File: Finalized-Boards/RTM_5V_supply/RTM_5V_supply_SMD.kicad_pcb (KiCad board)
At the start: 4 copper layers, 18.5 x 99 mm, 12 parts, among them J1 86093968114755V1LF

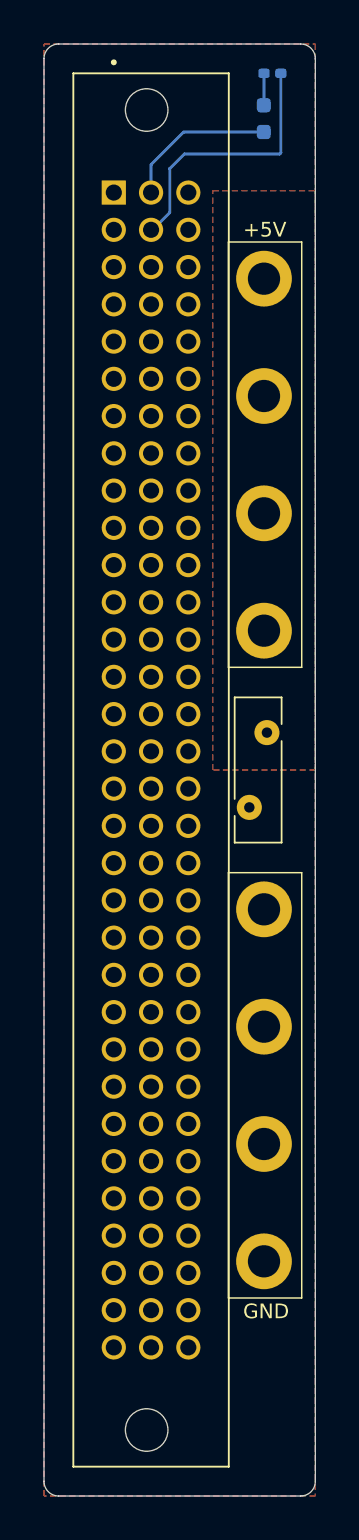
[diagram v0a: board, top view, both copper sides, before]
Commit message: Apply Matt's review changes to RTM, fanout and SRAM boards
SRAM: serial -> IDL_26_007 RevC - 09/2026 - CK/RS; vias untented (board-level);
GND zone 0.4 clearance / 0.1524 min width; In2 +3.3V stripe pulled back from
both board edges (tips 103.25 / 126.05) with 45-degree miters; +3.3V via moved
to (165.54, 125.92) and re-routed on F.Cu/B.Cu to clear GND (was 2 DRC errors);
C1/C2 0402 -> 0603 X7R in schematic and PCB; orphan teardrop + 2 zero-length
tracks removed.
Fanout: Matt's reworked layout (12 AWG input centred, both-side labels, 3 mm
shorter test points, D1/R1 as real reference designators, silk moved clear).
RTM: four 1812 1 A PPTCs, one per output; +5V pour full-board on F.Cu/In2,
GND on B.Cu/In1; 3.4 mm fused traces; zones extended past Edge.Cuts.
Removed stale pre-review gerbers/drills/layer PDFs (duplicates of Chris-Originals).
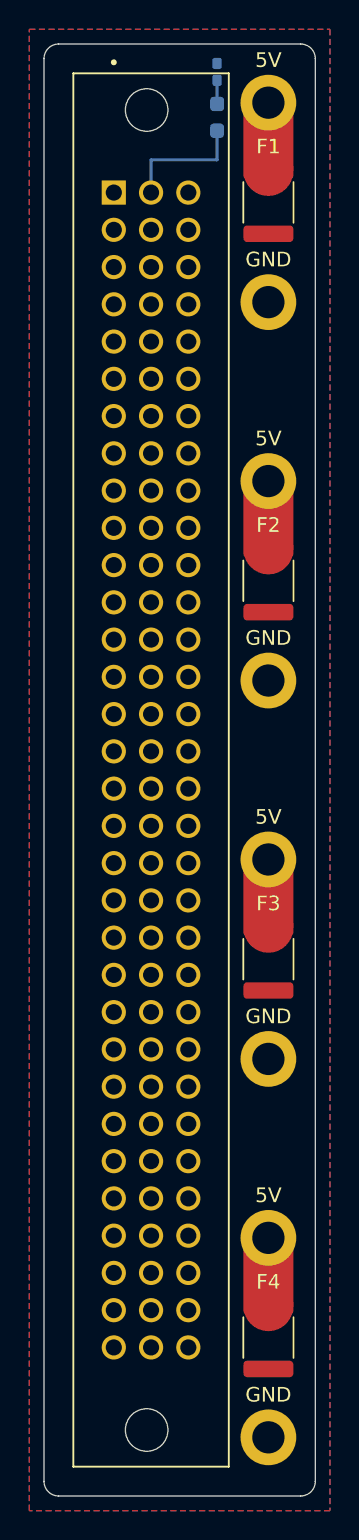
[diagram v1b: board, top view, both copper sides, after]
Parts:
- removed +5VP, GND: MountingHole_Pad, 1_My_footprint_lib:PTH_12AWG
- added +5VP1: SolderWire_PTH, 1_My_footprint_lib:PTH_12AWG, F.Cu at (108.0, 54.5)
- added F1: Polyfuse, Fuse:Fuse_1812_4532Metric, F.Cu at (108.0, 61.3)
- added F3: Polyfuse, Fuse:Fuse_1812_4532Metric, F.Cu at (108.0, 112.9)
- added F4: Polyfuse, Fuse:Fuse_1812_4532Metric, F.Cu at (108.0, 138.7)
- added GND1: SolderWire_PTH, 1_My_footprint_lib:PTH_12AWG, F.Cu at (108.0, 68.1)
- F2: footprint Fuse:Fuse_Bourns_MF-RHT100 -> Fuse:Fuse_1812_4532Metric
- moved +5VP4 41.4 mm to (108.0, 131.9)
- moved +5VP3 23.6 mm to (108.0, 106.1)
- moved GND2 23.6 mm to (108.0, 93.9)
- moved F2 15.5 mm to (108.0, 87.1)
- moved GND4 12.0 mm to (108.0, 145.5)
- moved +5VP2 5.81 mm to (108.0, 80.3)
- moved GND3 5.81 mm to (108.0, 119.7)
- moved D1 3.77 mm to (104.5, 52.4), turned to -90 degrees
- moved R1 3.19 mm to (104.5, 55.5)
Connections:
- +5VP2 pad 1: +5VP -> Net-(+5VP2-Pad1)
- +5VP3 pad 1: +5VP -> Net-(+5VP3-Pad1)
- +5VP4 pad 1: +5VP -> Net-(+5VP4-Pad1)
- F2 pad 2: +5VP -> Net-(+5VP2-Pad1)
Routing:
- net GND: track 18.2 -> 0.00 mm
- net Net-(+5VP3-Pad1): track 0.00 -> 4.66 mm
- net Net-(+5VP2-Pad1): track 0.00 -> 4.66 mm
- net Net-(+5VP1-Pad1): track 0.00 -> 4.66 mm
- net Net-(+5VP4-Pad1): track 0.00 -> 4.66 mm
- net +5V: track 10.5 -> 8.72 mm
- net Net-(D1-A): track 2.18 -> 1.62 mm
- removed copper zone on B.Cu, net +5VP
- removed copper zone on F.Cu, net +5VP
- removed copper zone on In1.Cu, net +5VP
- removed copper zone on In2.Cu, net +5VP
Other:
- board text added: "1"
- board text added: "2"
- board text added: "2026-09"
- board text added: "3"
- board text added: "4"
- board text added: "5V"
- board text added: "CK/RS"
- board text added: "F1"
- board text added: "F3"
- board text added: "F4"
- board text added: "RTM 5V revB"
- board text removed: "+5V"
- board text removed: "J1"

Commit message: Matt follow-up: 3.3V zone 0.4 clearance, silk-over-copper ignored, RTM IDL_26_026 silkscreen, fuse part MF-MSMF110/16-2
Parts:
- F1, F2, F3, F4: value Polyfuse -> MF-MSMF110/16-2
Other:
- board text added: "IDL_26_026 - KLM RTM 5V revB - 2026-09 - CK/RS"
- board text removed: "2026-09"
- board text removed: "CK/RS"
- board text removed: "RTM 5V revB"
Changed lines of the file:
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@@
 			)
 		)
-		(property "Value" "Polyfuse"
+		(property "Value" "MF-MSMF110/16-2"
 			(at 0 2.65 90)
 			(layer "F.Fab")
@@
 			)
 		)
-		(property "Value" "Polyfuse"
+		(property "Value" "MF-MSMF110/16-2"
 			(at 0 2.65 90)
 			(layer "F.Fab")
@@
 			)
 		)
-		(property "Value" "Polyfuse"
+		(property "Value" "MF-MSMF110/16-2"
 			(at 0 2.65 90)
 			(layer "F.Fab")
@@
 			)
 		)
-		(property "Value" "Polyfuse"
+		(property "Value" "MF-MSMF110/16-2"
 			(at 0 2.65 90)
 			(layer "F.Fab")
@@
 		(layer "User.1")
 	)
+	(gr_text "IDL_26_026 - KLM RTM 5V revB - 2026-09 - CK/RS"
+		(at 94.5 100 90)
+		(layer "B.SilkS")
+		(effects
+			(font
+				(size 1 1)
+				(thickness 0.15)
+			)
+			(justify mirror)
+		)
+	)
 	(gr_text "5V"
 		(at 108 51.6 0)
@@
 		)
 	)
-	(gr_text "RTM 5V revB"
-		(at 99.3 141.3 0)
-		(layer "B.SilkS")
-		(effects
-			(font
-				(size 1 1)
-				(thickness 0.15)
-			)
-			(justify mirror)
-		)
-	)
-	(gr_text "CK/RS"
-		(at 100.7 142.7 0)
-		(layer "B.SilkS")
-		(effects
-			(font
-				(size 1 1)
-				(thickness 0.15)
-			)
-			(justify mirror)
-		)
-	)
-	(gr_text "2026-09"
-		(at 101.8 148.3 0)
-		(layer "B.SilkS")
-		(effects
-			(font
-				(size 1 1)
-				(thickness 0.15)
-			)
-			(justify mirror)
-		)
-	)
